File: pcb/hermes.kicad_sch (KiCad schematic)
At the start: 16 parts, among them J1 OLED_128x64, U1 XIAO-RP2040-DIP, U2 MAX30102, U3 VL53L1CXV0FY1

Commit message: Added I2C pullups in schematic
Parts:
- added R5, R6: 4.7k, Resistor_SMD:R_0805_2012Metric, symbol Device:R
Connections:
- net +3V3: now also R5.1, R6.1
- net SCL: now also R5.2
- net SDA: now also R6.2

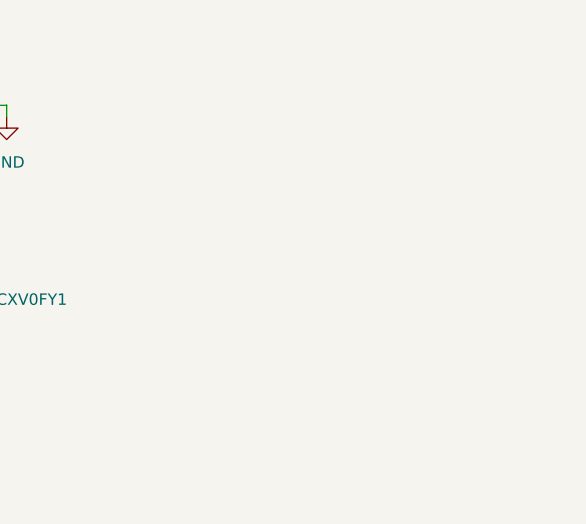
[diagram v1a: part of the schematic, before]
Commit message: Convert to ToF devboard (use previous versions for full Hermes board
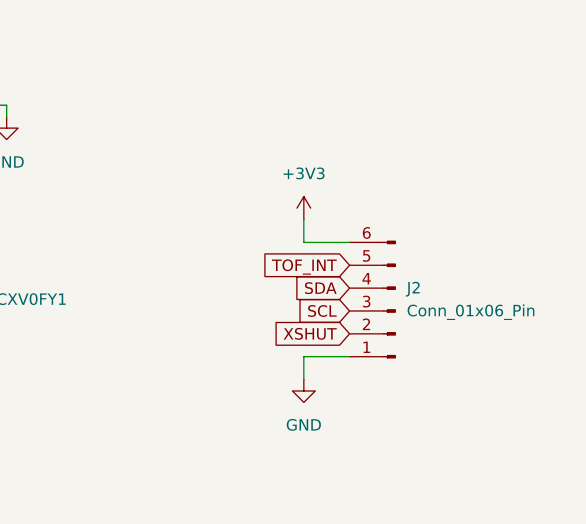
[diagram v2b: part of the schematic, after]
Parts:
- added J2: Conn_01x06_Pin, Connector_PinHeader_1.00mm:PinHeader_1x06_P1.00mm_Vertical, symbol Connector:Conn_01x06_Pin
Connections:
- net +3V3: now also J2.6 (Pin_6)
- net GND: now also J2.1 (Pin_1)
- net SCL: now also J2.3 (Pin_3)
- net SDA: now also J2.4 (Pin_4)
- net TOF_INT: now also J2.5 (Pin_5)
- net XSHUT: now also J2.2 (Pin_2)
